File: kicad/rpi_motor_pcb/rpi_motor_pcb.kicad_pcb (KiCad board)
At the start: 2 copper layers, 66.5 x 84.5 mm, 65 parts, among them J1 Raspberry_Pi_2_3, J10 CAN, J11 A-, J12 Motor C, J13 B-, J14 C-, J15 Y-, J16 Z-, J2 Motor Y, J3 Motor B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

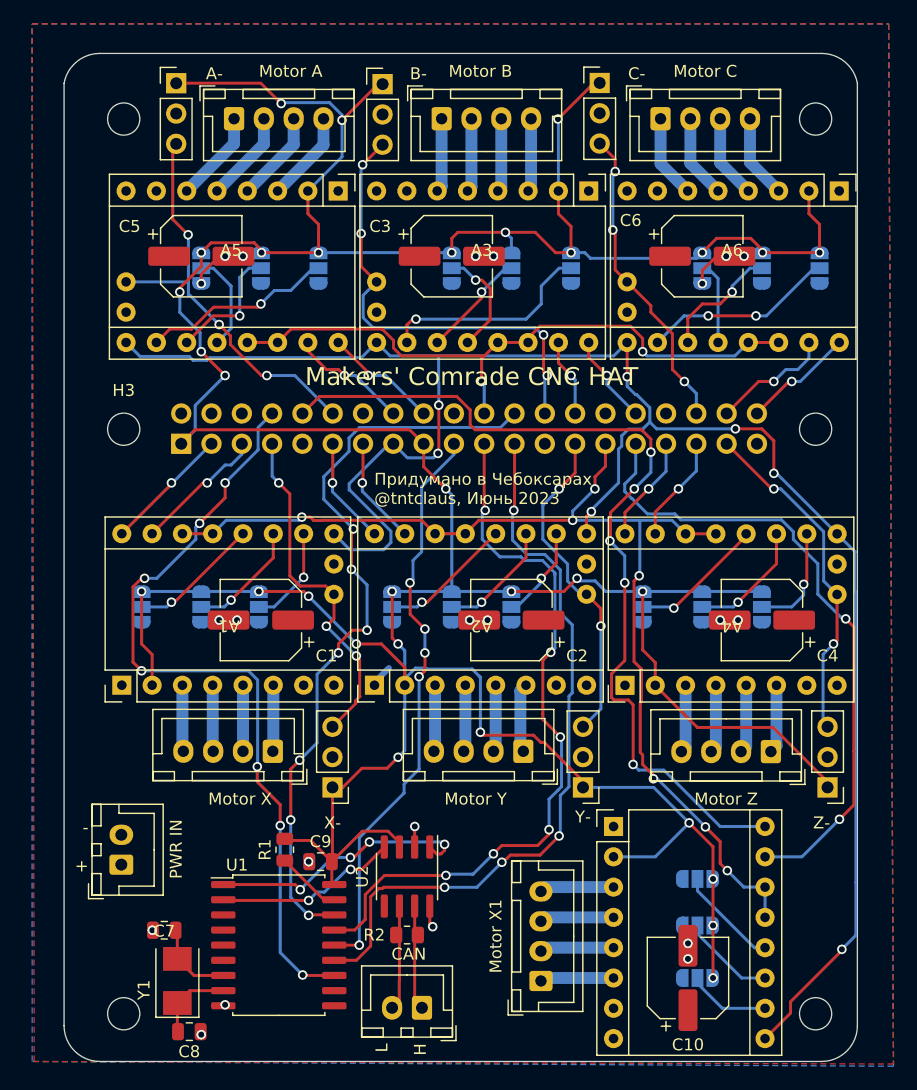
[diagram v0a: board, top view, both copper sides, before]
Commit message: rpi_motor_pcb: 6 axis version
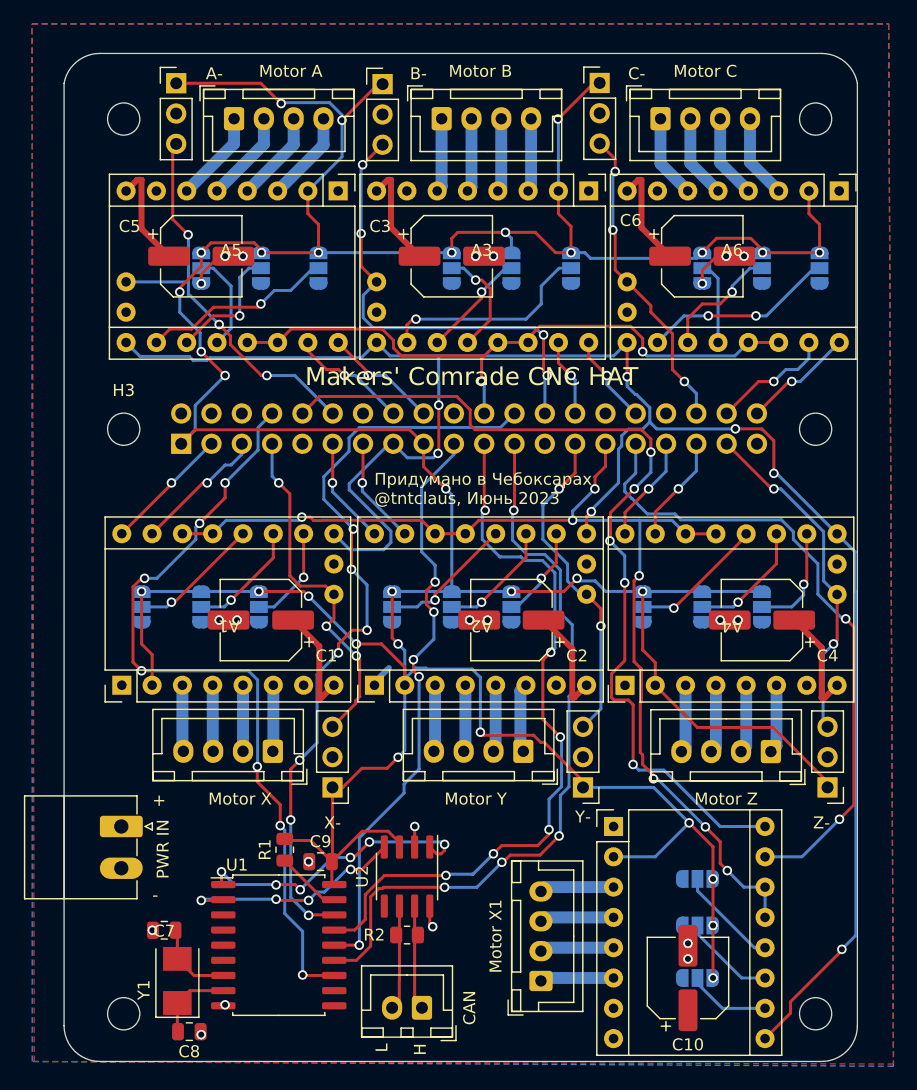
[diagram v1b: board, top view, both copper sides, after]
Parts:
- J4: footprint Connector_JST:JST_XH_B2B-XH-A_1x02_P2.50mm_Vertical -> Connector_Phoenix_MC:PhoenixContact_MC_1,5_2-G-3.5_1x02_P3.50mm_Horizontal
- moved J4 3.20 mm to (27.8, 80.3), turned to -90 degrees
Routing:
- net Vin: track 0.00 -> 54.6 mm
- net /CAN/RX: track 15.4 -> 19.2 mm, vias 2 -> 4
- net /CAN/TX: track 22.6 -> 24.3 mm, vias 4 -> 6
- net /CAN_MOSI: track 48.4 -> 49.3 mm
- net /CAN_MISO: track 61.9 -> 61.4 mm
